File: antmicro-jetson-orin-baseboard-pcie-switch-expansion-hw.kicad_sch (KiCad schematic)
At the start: 10 parts

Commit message: [#100765] WIP: Apply review changes
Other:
- sheet OCuLink ports: added {I_{2}C}; removed none
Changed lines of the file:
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@@
+	)
+	(junction
+		(at 185.42 144.78)
+		(diameter 0)
+		(color 0 0 0 0)
 	)
 	(junction
@@
 		)
 	)
+	(bus
+		(pts
+			(xy 304.8 142.24) (xy 304.8 180.34)
+		)
+		(stroke
+			(width 0)
+			(type default)
+		)
+	)
+	(bus
+		(pts
+			(xy 304.8 180.34) (xy 185.42 180.34)
+		)
+		(stroke
+			(width 0)
+			(type default)
+		)
+	)
 	(wire
 		(pts
@@
 		)
 	)
+	(bus
+		(pts
+			(xy 299.72 142.24) (xy 304.8 142.24)
+		)
+		(stroke
+			(width 0)
+			(type default)
+		)
+	)
 	(wire
 		(pts
@@
 		(pts
 			(xy 40.64 241.3) (xy 40.64 247.65)
+		)
+		(stroke
+			(width 0)
+			(type default)
+		)
+	)
+	(bus
+		(pts
+			(xy 185.42 180.34) (xy 185.42 144.78)
 		)
 		(stroke
@@
 			)
 		)
+		(pin "{I_{2}C}" bidirectional
+			(at 299.72 142.24 0)
+			(effects
+				(font
+					(size 1.27 1.27)
+				)
+				(justify right)
+			)
+		)

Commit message: [#100765] Apply fixes from review
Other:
- removed sheet Tag Connect, EEPROM
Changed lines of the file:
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@@
 	(title_block
 		(title "antmicro-jetson-orin-baseboard-pcie-switch-expansion-hw")
-		(date "10.07.2026")
+		(date "2026-07-23")
 		(rev "1.0.0")
 		(company "Antmicro")
@@
 	(bus
 		(pts
-			(xy 191.77 135.89) (xy 194.31 135.89)
+			(xy 228.6 128.27) (xy 240.03 128.27)
 		)
 		(stroke
@@
 	(bus
 		(pts
-			(xy 228.6 128.27) (xy 240.03 128.27)
+			(xy 228.6 135.89) (xy 232.41 135.89)
+		)
+		(stroke
+			(width 0)
+			(type default)
+		)
+	)
+	(wire
+		(pts
+			(xy 179.07 137.16) (xy 179.07 154.94)
 		)
 		(stroke
@@
 	(bus
 		(pts
-			(xy 191.77 106.68) (xy 191.77 135.89)
+			(xy 167.64 133.35) (xy 185.42 133.35)
+		)
+		(stroke
+			(width 0)
+			(type default)
+		)
+	)
+	(wire
+		(pts
+			(xy 40.64 234.95) (xy 40.64 241.3)
 		)
 		(stroke
@@
 	(bus
 		(pts
-			(xy 189.23 97.79) (xy 189.23 139.7)
+			(xy 274.32 154.94) (xy 274.32 161.29)
 		)
 		(stroke
@@
 	(bus
 		(pts
-			(xy 228.6 135.89) (xy 232.41 135.89)
-		)
-		(stroke
-			(width 0)
-			(type default)
-		)
-	)
-	(wire
-		(pts
-			(xy 179.07 137.16) (xy 179.07 154.94)
+			(xy 232.41 151.13) (xy 240.03 151.13)
+		)
+		(stroke
+			(width 0)
+			(type default)
+		)
+	)
+	(wire
+		(pts
+			(xy 40.64 254) (xy 40.64 260.35)
 		)
 		(stroke
@@
 	(bus
 		(pts
-			(xy 167.64 133.35) (xy 185.42 133.35)
-		)
-		(stroke
-			(width 0)
-			(type default)
-		)
-	)
-	(wire
-		(pts
-			(xy 40.64 234.95) (xy 40.64 241.3)
+			(xy 304.8 142.24) (xy 304.8 180.34)
 		)
 		(stroke
@@
 	(bus
 		(pts
-			(xy 274.32 154.94) (xy 274.32 161.29)
+			(xy 304.8 180.34) (xy 185.42 180.34)
+		)
+		(stroke
+			(width 0)
+			(type default)
+		)
+	)
+	(wire
+		(pts
+			(xy 40.64 222.25) (xy 40.64 228.6)
 		)
 		(stroke
@@
 	(bus
 		(pts
-			(xy 195.58 97.79) (xy 189.23 97.79)
+			(xy 167.64 129.54) (xy 194.31 129.54)
 		)
 		(stroke
@@
 	(bus
 		(pts
-			(xy 232.41 151.13) (xy 240.03 151.13)
-		)
-		(stroke
-			(width 0)
-			(type default)
-		)
-	)
-	(wire
-		(pts
-			(xy 40.64 254) (xy 40.64 260.35)
+			(xy 299.72 142.24) (xy 304.8 142.24)
+		)
+		(stroke
+			(width 0)
+			(type default)
+		)
+	)
+	(wire
+		(pts
+			(xy 40.64 241.3) (xy 41.91 241.3)
 		)
 		(stroke
@@
 	(bus
 		(pts
-			(xy 304.8 142.24) (xy 304.8 180.34)
+			(xy 274.32 142.24) (xy 274.32 147.32)
+		)
+		(stroke
+			(width 0)
+			(type default)
+		)
+	)
+	(wire
+		(pts
+			(xy 40.64 228.6) (xy 40.64 234.95)
+		)
+		(stroke
+			(width 0)
+			(type default)
+		)
+	)
+	(wire
+		(pts
+			(xy 40.64 228.6) (xy 41.91 228.6)
+		)
+		(stroke
+			(width 0)
+			(type default)
+		)
+	)
+	(wire
+		(pts
+			(xy 41.91 266.7) (xy 40.64 266.7)
+		)
+		(stroke
+			(width 0)
+			(type default)
+		)
+	)
+	(wire
+		(pts
+			(xy 167.64 137.16) (xy 179.07 137.16)
+		)
+		(stroke
+			(width 0)
+			(type default)
+		)
+	)
+	(wire
+		(pts
+			(xy 179.07 154.94) (xy 240.03 154.94)
+		)
+		(stroke
+			(width 0)
+			(type default)
+		)
+	)
+	(wire
+		(pts
+			(xy 40.64 254) (xy 41.91 254)
 		)
 		(stroke
@@
 	(bus
 		(pts
-			(xy 304.8 180.34) (xy 185.42 180.34)
-		)
-		(stroke
-			(width 0)
-			(type default)
-		)
-	)
-	(wire
-		(pts
-			(xy 40.64 222.25) (xy 40.64 228.6)
-		)
-		(stroke
-			(width 0)
-			(type default)
-		)
-	)
-	(bus
-		(pts
-			(xy 167.64 129.54) (xy 194.31 129.54)
-		)
-		(stroke
-			(width 0)
-			(type default)
-		)
-	)
-	(bus
-		(pts
-			(xy 299.72 142.24) (xy 304.8 142.24)
-		)
-		(stroke
-			(width 0)
-			(type default)
-		)
-	)
-	(wire
-		(pts
-			(xy 40.64 241.3) (xy 41.91 241.3)
-		)
-		(stroke
-			(width 0)
-			(type default)
-		)
-	)
-	(bus
-		(pts
-			(xy 274.32 142.24) (xy 274.32 147.32)
-		)
-		(stroke
-			(width 0)
-			(type default)
-		)
-	)
-	(wire
-		(pts
-			(xy 40.64 228.6) (xy 40.64 234.95)
-		)
-		(stroke
-			(width 0)
-			(type default)
-		)
-	)
-	(wire
-		(pts
-			(xy 40.64 228.6) (xy 41.91 228.6)
-		)
-		(stroke
-			(width 0)
-			(type default)
-		)
-	)
-	(wire
-		(pts
-			(xy 41.91 266.7) (xy 40.64 266.7)
-		)
-		(stroke
-			(width 0)
-			(type default)
-		)
-	)
-	(wire
-		(pts
-			(xy 167.64 137.16) (xy 179.07 137.16)
-		)
-		(stroke
-			(width 0)
-			(type default)
-		)
-	)
-	(wire
-		(pts
-			(xy 179.07 154.94) (xy 240.03 154.94)
-		)
-		(stroke
-			(width 0)
-			(type default)
-		)
-	)
-	(wire
-		(pts
-			(xy 40.64 254) (xy 41.91 254)
-		)
-		(stroke
-			(width 0)
-			(type default)
-		)
-	)
-	(bus
-		(pts
 			(xy 274.32 147.32) (xy 270.51 147.32)
 		)
@@
 		(pts
 			(xy 40.64 222.25) (xy 41.91 222.25)
-		)
-		(stroke
-			(width 0)
-			(type default)
-		)
-	)
-	(bus
-		(pts
-			(xy 195.58 106.68) (xy 191.77 106.68)
 		)
 		(stroke
@@
 				)
 			)
-		)
-	)
-	(sheet
-		(at 195.58 91.44)
-		(size 21.59 17.78)
-		(exclude_from_sim no)
-		(in_bom yes)
-		(on_board yes)
-		(dnp no)
-		(fields_autoplaced yes)
-		(stroke
-			(width 0.1524)
-			(type solid)
-		)
-		(fill
-			(color 0 0 0 0)
-		)
-		(property "Sheetname" "Tag Connect, EEPROM"
-			(at 195.58 90.7284 0)
-			(show_name no)
-			(do_not_autoplace no)
-			(effects
-				(font
-					(size 1.27 1.27)
-				)
-				(justify left bottom)
-			)
-		)
-		(property "Sheetfile" "eeprom_tagconnect.kicad_sch"
-			(at 195.58 109.8046 0)
-			(show_name no)
-			(do_not_autoplace no)
-			(effects
-				(font
-					(size 1.27 1.27)
-				)
-				(justify left top)
-			)
-		)
-		(pin "{SPI}" bidirectional
-			(at 195.58 106.68 180)
-			(effects
-				(font
-					(size 1.27 1.27)
-				)
-				(justify left)
-			)
-		)
-		(pin "{JTAG}" bidirectional
-			(at 195.58 97.79 180)
-			(effects
-				(font
-					(size 1.27 1.27)
-				)
-				(justify left)
-			)
-		)
-		(instances
-			(project "antmicro-jetson-orin-baseboard-pcie-switch-expansion-hw"
-				(path "/9f8272ef-d62d-4578-9094-a2852fcd4bf4"
-					(page "9")
-				)
-			)

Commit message: [#100765] Update top sheet
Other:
- sheet PCIe Switch ports: added none; removed {JTAG}, {SPI}
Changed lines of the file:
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@@
+	)
+	(junction
+		(at 185.42 133.35)
+		(diameter 0)
+		(color 0 0 0 0)
 	)
 	(junction
@@
 	)
 	(junction
-		(at 185.42 144.78)
-		(diameter 0)
-		(color 0 0 0 0)
-	)
-	(junction
 		(at 40.64 260.35)
 		(diameter 0)
@@
 		)
 	)
+	(wire
+		(pts
+			(xy 40.64 266.7) (xy 40.64 270.51)
+		)
+		(stroke
+			(width 0)
+			(type default)
+		)
+	)
 	(bus
 		(pts
-			(xy 189.23 139.7) (xy 194.31 139.7)
-		)
-		(stroke
-			(width 0)
-			(type default)
-		)
-	)
-	(wire
-		(pts
-			(xy 40.64 266.7) (xy 40.64 270.51)
+			(xy 270.51 154.94) (xy 274.32 154.94)
 		)
 		(stroke
@@
 	(bus
 		(pts
-			(xy 185.42 133.35) (xy 185.42 144.78)
+			(xy 185.42 133.35) (xy 194.31 133.35)
+		)
+		(stroke
+			(width 0)
+			(type default)
+		)
+	)
+	(wire
+		(pts
+			(xy 173.99 165.1) (xy 194.31 165.1)
 		)
 		(stroke
@@
 	(bus
 		(pts
-			(xy 270.51 154.94) (xy 274.32 154.94)
+			(xy 185.42 133.35) (xy 185.42 180.34)
+		)
+		(stroke
+			(width 0)
+			(type default)
+		)
+	)
+	(wire
+		(pts
+			(xy 40.64 247.65) (xy 41.91 247.65)
 		)
 		(stroke
@@
 	(bus
 		(pts
-			(xy 185.42 144.78) (xy 194.31 144.78)
-		)
-		(stroke
-			(width 0)
-			(type default)
-		)
-	)
-	(wire
-		(pts
-			(xy 173.99 165.1) (xy 194.31 165.1)
-		)
-		(stroke
-			(width 0)
-			(type default)
-		)
-	)
-	(wire
-		(pts
-			(xy 40.64 247.65) (xy 41.91 247.65)
+			(xy 231.14 134.62) (xy 231.14 151.13)
+		)
+		(stroke
+			(width 0)
+			(type default)
+		)
+	)
+	(wire
+		(pts
+			(xy 40.64 234.95) (xy 41.91 234.95)
 		)
 		(stroke
@@
 	(bus
 		(pts
-			(xy 232.41 135.89) (xy 232.41 151.13)
-		)
-		(stroke
-			(width 0)
-			(type default)
-		)
-	)
-	(wire
-		(pts
-			(xy 40.64 234.95) (xy 41.91 234.95)
+			(xy 278.13 142.24) (xy 274.32 142.24)
 		)
 		(stroke
@@
 	(bus
 		(pts
-			(xy 278.13 142.24) (xy 274.32 142.24)
+			(xy 228.6 128.27) (xy 240.03 128.27)
 		)
 		(stroke
@@
 	(bus
 		(pts
-			(xy 228.6 128.27) (xy 240.03 128.27)
+			(xy 228.6 134.62) (xy 231.14 134.62)
+		)
+		(stroke
+			(width 0)
+			(type default)
+		)
+	)
+	(wire
+		(pts
+			(xy 179.07 137.16) (xy 179.07 154.94)
 		)
 		(stroke
@@
 	(bus
 		(pts
-			(xy 228.6 135.89) (xy 232.41 135.89)
-		)
-		(stroke
-			(width 0)
-			(type default)
-		)
-	)
-	(wire
-		(pts
-			(xy 179.07 137.16) (xy 179.07 154.94)
+			(xy 167.64 133.35) (xy 185.42 133.35)
+		)
+		(stroke
+			(width 0)
+			(type default)
+		)
+	)
+	(wire
+		(pts
+			(xy 40.64 234.95) (xy 40.64 241.3)
 		)
 		(stroke
@@
 	(bus
 		(pts
-			(xy 167.64 133.35) (xy 185.42 133.35)
-		)
-		(stroke
-			(width 0)
-			(type default)
-		)
-	)
-	(wire
-		(pts
-			(xy 40.64 234.95) (xy 40.64 241.3)
+			(xy 274.32 154.94) (xy 274.32 161.29)
 		)
 		(stroke
@@
 	(bus
 		(pts
-			(xy 274.32 154.94) (xy 274.32 161.29)
+			(xy 231.14 151.13) (xy 240.03 151.13)
+		)
+		(stroke
+			(width 0)
+			(type default)
+		)
+	)
+	(wire
+		(pts
+			(xy 40.64 254) (xy 40.64 260.35)
 		)
 		(stroke
@@
 	(bus
 		(pts
-			(xy 232.41 151.13) (xy 240.03 151.13)
-		)
-		(stroke
-			(width 0)
-			(type default)
-		)
-	)
-	(wire
-		(pts
-			(xy 40.64 254) (xy 40.64 260.35)
+			(xy 304.8 142.24) (xy 304.8 180.34)
 		)
 		(stroke
@@
 	(bus
 		(pts
-			(xy 304.8 142.24) (xy 304.8 180.34)
+			(xy 304.8 180.34) (xy 185.42 180.34)
+		)
+		(stroke
+			(width 0)
+			(type default)
+		)
+	)
+	(wire
+		(pts
+			(xy 40.64 222.25) (xy 40.64 228.6)
 		)
 		(stroke
@@
 	(bus
 		(pts
-			(xy 304.8 180.34) (xy 185.42 180.34)
-		)
-		(stroke
-			(width 0)
-			(type default)
-		)
-	)
-	(wire
-		(pts
-			(xy 40.64 222.25) (xy 40.64 228.6)
+			(xy 167.64 129.54) (xy 194.31 129.54)
 		)
 		(stroke
@@
 	(bus
 		(pts
-			(xy 167.64 129.54) (xy 194.31 129.54)
+			(xy 299.72 142.24) (xy 304.8 142.24)
+		)
+		(stroke
+			(width 0)
+			(type default)
+		)
+	)
+	(wire
+		(pts
+			(xy 40.64 241.3) (xy 41.91 241.3)
 		)
 		(stroke
@@
 	(bus
 		(pts
-			(xy 299.72 142.24) (xy 304.8 142.24)
-		)
-		(stroke
-			(width 0)
-			(type default)
-		)
-	)
-	(wire
-		(pts
-			(xy 40.64 241.3) (xy 41.91 241.3)
+			(xy 274.32 142.24) (xy 274.32 147.32)
+		)
+		(stroke
+			(width 0)
+			(type default)
+		)
+	)
+	(wire
+		(pts
+			(xy 40.64 228.6) (xy 40.64 234.95)
+		)
+		(stroke
+			(width 0)
+			(type default)
+		)
+	)
+	(wire
+		(pts
+			(xy 40.64 228.6) (xy 41.91 228.6)
+		)
+		(stroke
+			(width 0)
+			(type default)
+		)
+	)
+	(wire
+		(pts
+			(xy 41.91 266.7) (xy 40.64 266.7)
+		)
+		(stroke
+			(width 0)
+			(type default)
+		)
+	)
+	(wire
+		(pts
+			(xy 167.64 137.16) (xy 179.07 137.16)
+		)
+		(stroke
+			(width 0)
+			(type default)
+		)
+	)
+	(wire
+		(pts
+			(xy 179.07 154.94) (xy 240.03 154.94)
+		)
+		(stroke
+			(width 0)
+			(type default)
+		)
+	)
+	(wire
+		(pts
+			(xy 40.64 254) (xy 41.91 254)
 		)
 		(stroke
@@
 	(bus
 		(pts
-			(xy 274.32 142.24) (xy 274.32 147.32)
-		)
-		(stroke
-			(width 0)
-			(type default)
-		)
-	)
-	(wire
-		(pts
-			(xy 40.64 228.6) (xy 40.64 234.95)
-		)
-		(stroke
-			(width 0)
-			(type default)
-		)
-	)
-	(wire
-		(pts
-			(xy 40.64 228.6) (xy 41.91 228.6)
-		)
-		(stroke
-			(width 0)
-			(type default)
-		)
-	)
-	(wire
-		(pts
-			(xy 41.91 266.7) (xy 40.64 266.7)
-		)
-		(stroke
-			(width 0)
-			(type default)
-		)
-	)
-	(wire
-		(pts
-			(xy 167.64 137.16) (xy 179.07 137.16)
-		)
-		(stroke
-			(width 0)
-			(type default)
-		)
-	)
-	(wire
-		(pts
-			(xy 179.07 154.94) (xy 240.03 154.94)
-		)
-		(stroke
-			(width 0)
-			(type default)
-		)
-	)
-	(wire
-		(pts
-			(xy 40.64 254) (xy 41.91 254)
-		)
-		(stroke
-			(width 0)
-			(type default)
-		)
-	)
-	(bus
-		(pts
 			(xy 274.32 147.32) (xy 270.51 147.32)
 		)
@@
 		(pts
 			(xy 40.64 241.3) (xy 40.64 247.65)
-		)
-		(stroke
-			(width 0)
-			(type default)
-		)
-	)
-	(bus
-		(pts
-			(xy 185.42 180.34) (xy 185.42 144.78)
 		)
 		(stroke
@@
 	(sheet
 		(at 194.31 124.46)
-		(size 34.29 24.13)
+		(size 34.29 15.24)
 		(exclude_from_sim no)
 		(in_bom yes)
@@
 		)
 		(property "Sheetfile" "pcie-switch.kicad_sch"
-			(at 194.31 149.1746 0)
+			(at 194.31 140.2846 0)
 			(show_name no)
 			(do_not_autoplace no)
@@
 		)
 		(pin "PCIe_{x2_1}{PCIe}" bidirectional
-			(at 228.6 135.89 0)
+			(at 228.6 134.62 0)
 			(effects
 				(font
@@
 		)
 		(pin "{I_{2}C}" bidirectional
-			(at 194.31 144.78 180)
-			(effects
-				(font
-					(size 1.27 1.27)
-				)
-				(justify left)
-			)
-		)
-		(pin "{SPI}" bidirectional
-			(at 194.31 135.89 180)
-			(effects
-				(font
-					(size 1.27 1.27)
-				)
-				(justify left)
-			)
-		)
-		(pin "{JTAG}" bidirectional
-			(at 194.31 139.7 180)
-			(effects
-				(font
+			(at 194.31 133.35 180)
+			(effects
+				(font

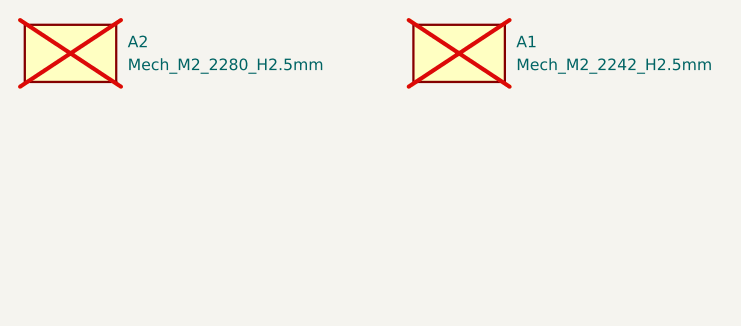
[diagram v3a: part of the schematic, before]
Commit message: [#100765] Reset designators
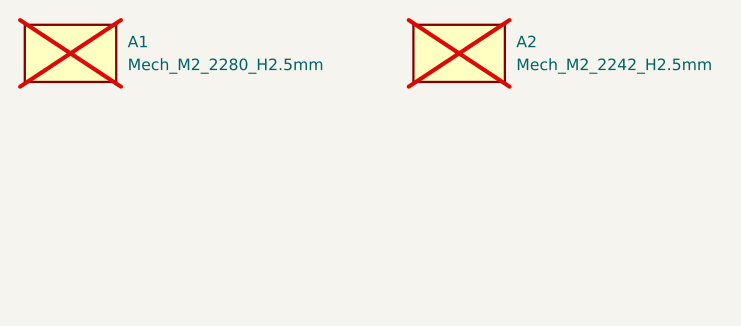
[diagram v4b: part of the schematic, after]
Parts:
- renumbered A2 to A1, A1 to A2
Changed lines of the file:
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@@
 		(dnp yes)
 		(fields_autoplaced yes)
-		(property "Reference" "A2"
+		(property "Reference" "A1"
 			(at 48.26 27.305 0)
 			(show_name no)
@@
 			(project "antmicro-jetson-orin-baseboard-pcie-switch-expansion-hw"
 				(path "/9f8272ef-d62d-4578-9094-a2852fcd4bf4"
-					(reference "A2")
+					(reference "A1")
 					(unit 1)
 				)
@@
 		(dnp yes)
 		(fields_autoplaced yes)
-		(property "Reference" "A1"
+		(property "Reference" "A2"
 			(at 91.44 27.305 0)
 			(show_name no)
@@
 			(project "antmicro-jetson-orin-baseboard-pcie-switch-expansion-hw"
 				(path "/9f8272ef-d62d-4578-9094-a2852fcd4bf4"
-					(reference "A1")
+					(reference "A2")
 					(unit 1)
 				)
@@
 		(dnp no)
 		(fields_autoplaced yes)
-		(property "Reference" "#PWR010"
+		(property "Reference" "#PWR01"
 			(at 49.53 273.05 0)
 			(hide yes)
@@
 			(project "antmicro-jetson-orin-baseboard-pcie-switch-expansion-hw"
 				(path "/9f8272ef-d62d-4578-9094-a2852fcd4bf4"
-					(reference "#PWR010")
+					(reference "#PWR01")
 					(unit 1)
 				)

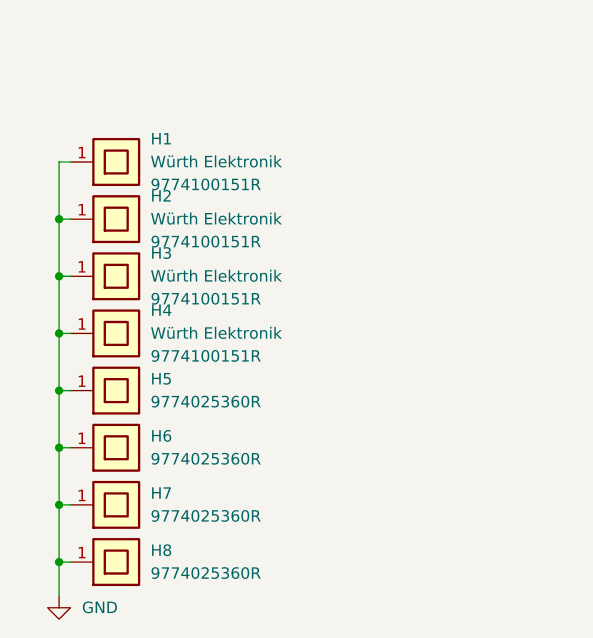
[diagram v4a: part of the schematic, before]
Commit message: [#100765] Fix legacy DNP & Remove obsolete spacer drills
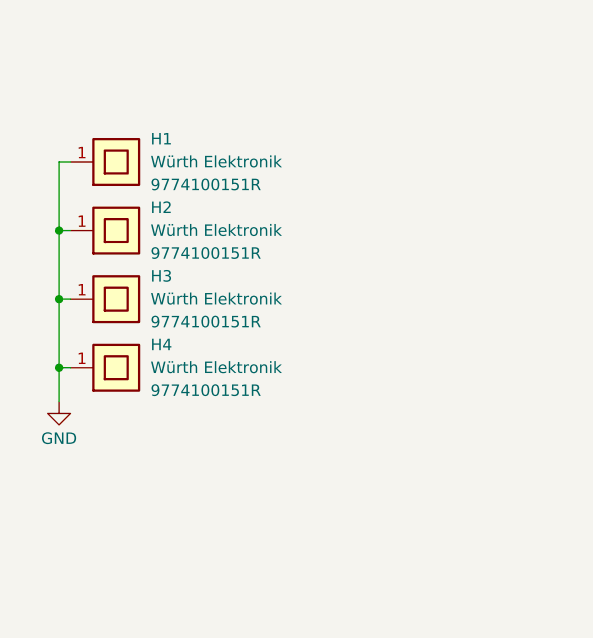
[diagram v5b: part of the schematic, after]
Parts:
- removed H5, H6, H7, H8: Spacer_Drill4.4mm_H2.5mm_9774025360R, antmicro-footprints:Spacer_Drill4.4mm_H2.5mm_9774025360R, symbol antmicroMechanicalParts:Spacer_Drill4.4mm_H2.5mm_9774025360R
- A1: now in the parts list
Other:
- moved on the sheet: H2, H3, H4
